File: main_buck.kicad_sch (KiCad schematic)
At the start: 13 parts, among them Q1 IRFB7730PBF, Q2 IRFB7730PBF, U1 IR2109, U2 LM317_TO-220

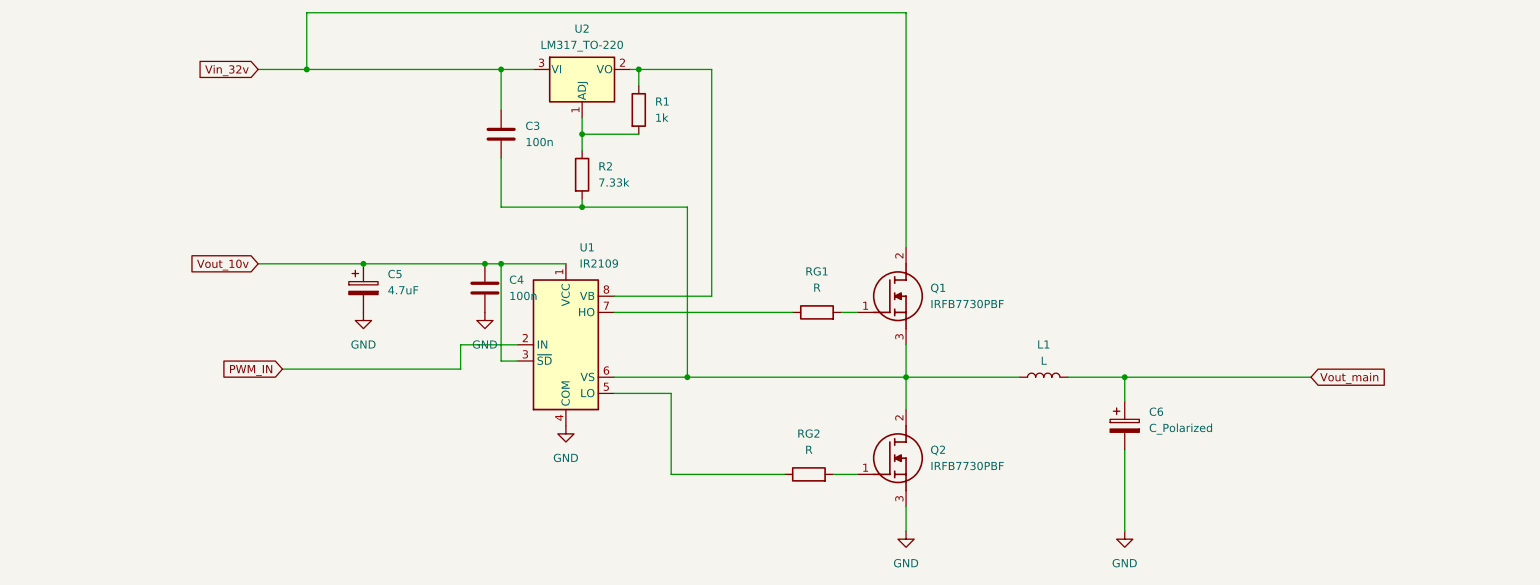
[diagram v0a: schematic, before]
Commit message: zmiana sekcji zasilania digital oraz drivera
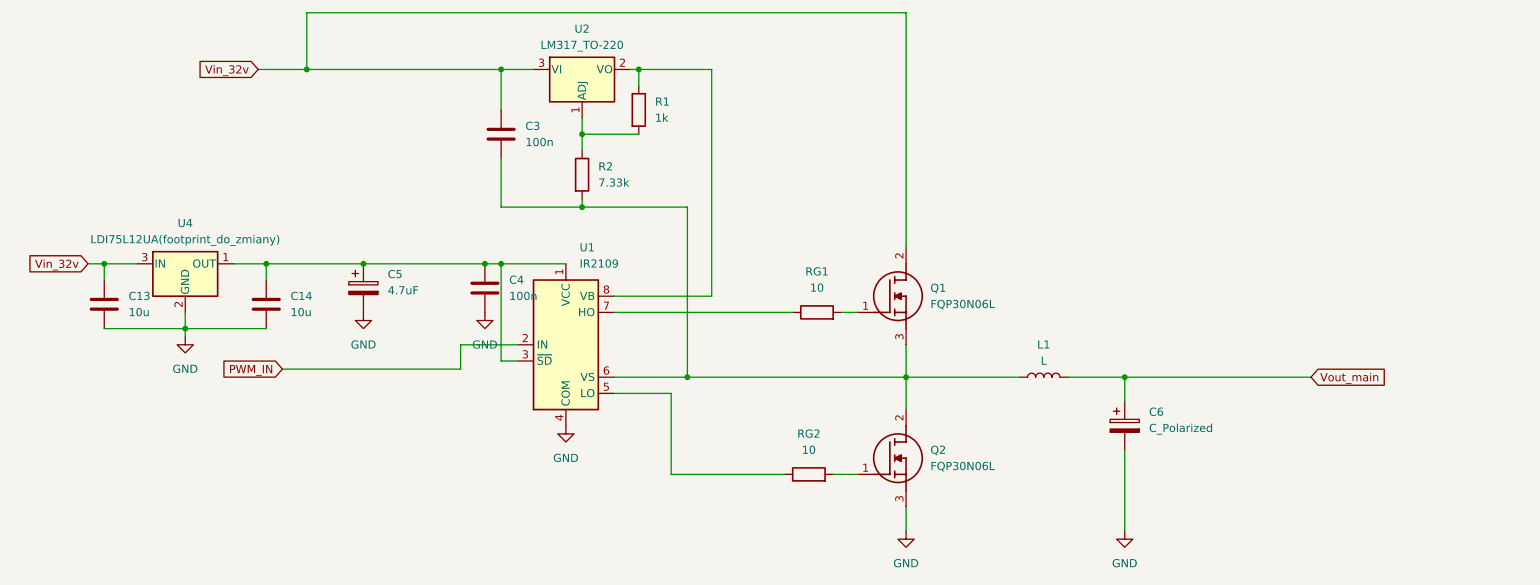
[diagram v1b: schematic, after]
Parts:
- added C13, C14: 10u, symbol Device:C
- added U4: LDI75L12UA(footprint_do_zmiany), Package_TO_SOT_SMD:SOT-89-3, symbol Regulator_Linear:L78L12_SOT89
- Q1, Q2: value IRFB7730PBF -> FQP30N06L
- RG1, RG2: value R -> 10
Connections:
- net GND: now also C13.2, C14.2, U4.2 (GND)
- net Vin_32v: now also C13.1, U4.3 (IN)
- net Vout_10v: no longer names the net of C4.1, C5.1, U1.1 (VCC), U1.3 (~{SD})
- net Vout_10v: now also C14.1, U4.1 (OUT)

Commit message: aktualizacja wartości cewki i kondensatora w przetwornicy głównej
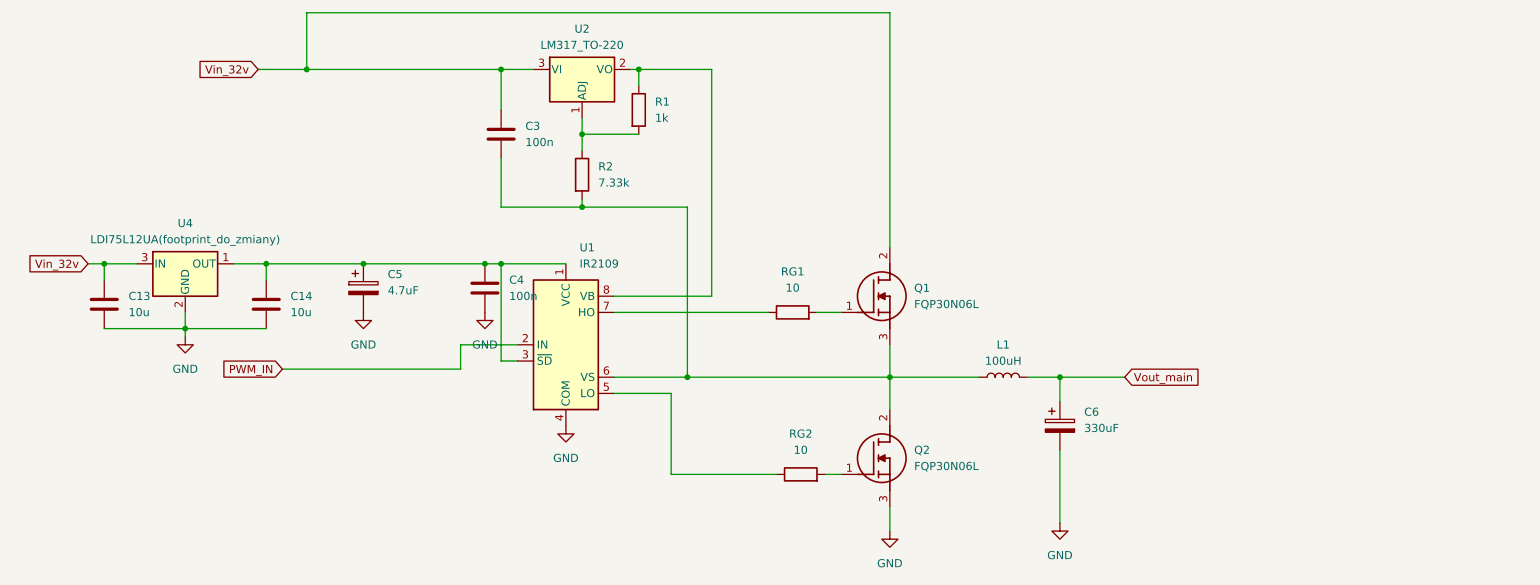
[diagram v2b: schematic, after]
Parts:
- C6: value C_Polarized -> 330uF
- L1: value L -> 100uH
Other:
- moved on the sheet: C6, L1, Q1, Q2, RG1, RG2

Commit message: dodanie testpointów, diody tvs, rezystora pomiarowego
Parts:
- added D3, D4: SMAJ12A, Diode_SMD:D_SMA, symbol Diode:SMAJ12A
- added R_i_mesure: 0.1, symbol Device:R
- added TP_przed_cewka, TP_za_cewka, Vout_main_+, Vout_main_-: Conn_01x01_Pin, symbol Connector:Conn_01x01_Pin
- added fuze_out: Fuse, symbol Device:Fuse
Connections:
- net GND: now also D3.2 (A2), R_i_mesure.1
- net Vout_main: now also fuze_out.2; no longer C6.1, L1.2
- net at C3.2, L1.1, Q1.3 (S)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: now also D4.2 (A2), TP_przed_cewka.1 (Pin_1)
- net at R1.1, U1.8 (VB), U2.2 (VO): now also D4.1 (A1)
- net at C14.1, C4.1, C5.1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: now also D3.1 (A1)
- new net OUT_GND_i_mesure: R_i_mesure.2, Vout_main_-.1 (Pin_1)
- new net Vinm: C6.1, L1.2, TP_za_cewka.1 (Pin_1), Vout_main_+.1 (Pin_1), fuze_out.1

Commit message: dodanie footprintów do main buck (jeszcze driver i razystor bramek) poprawiony pinout LDI75L12UA, dodane footprinty do digital power
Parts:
- removed U2: LM317_TO-220, Package_TO_SOT_THT:TO-220-3_Vertical, symbol Regulator_Linear:LM317_TO-220
- removed U4: LDI75L12UA(footprint_do_zmiany), Package_TO_SOT_SMD:SOT-89-3, symbol Regulator_Linear:L78L12_SOT89
- added U4: LM317_TO-263, Package_TO_SOT_SMD:TO-263-2, symbol Regulator_Linear:LM317_TO-263
- added U8: LDI75L12UA, Package_TO_SOT_SMD:SOT-89-3_Handsoldering, symbol Regulator_Linear:L78L12_SOT89
- C13, C14, C3, C4: footprint (none) -> Capacitor_SMD:C_0805_2012Metric_Pad1.18x1.45mm_HandSolder
- C5: footprint (none) -> Capacitor_SMD:CP_Elec_4x5.8
- C6: footprint (none) -> Capacitor_SMD:CP_Elec_18x17.5
- L1: footprint (none) -> Inductor_THT:L_Toroid_Vertical_L41.9mm_W19.1mm_P15.80mm_Vishay_TJ7
- Q1, Q2: footprint TO254P483X1016X1994-3P -> Package_TO_SOT_THT:TO-220-3_Vertical
- R1, R2: footprint (none) -> Resistor_SMD:R_0805_2012Metric_Pad1.20x1.40mm_HandSolder
- R_i_mesure: footprint (none) -> Resistor_SMD:R_2512_6332Metric_Pad1.40x3.35mm_HandSolder
- TP_przed_cewka, TP_za_cewka: footprint (none) -> Connector_PinHeader_2.54mm:PinHeader_1x01_P2.54mm_Vertical
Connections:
- net GND: now also U8.1 (GND)
- net Vin_32v: now also U4.3 (VI), U8.2 (IN)
- net at D4.1 (A1), R1.1, U1.8 (VB): now also U4.2 (VO)
- net at R1.2, R2.1: now also U4.1 (ADJ)
- net at C14.1, C4.1, C5.1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: now also U8.3 (OUT)

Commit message: Dodanie brakującego połączenia do przycisków enkoderów
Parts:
- renumbered R_i_mesure to R_i_mesure1, TP_przed_cewka to TP_przed_cewka1, TP_za_cewka to TP_za_cewka1, Vout_main_+ to Vout_main_+1, Vout_main_- to Vout_main_-1, fuze_out to fuze_out1
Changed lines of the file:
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@@
 		(dnp no)
 		(fields_autoplaced yes)
-		(property "Reference" "#PWR?"
+		(property "Reference" "#PWR029"
 			(at 80.01 80.01 0)
 			(hide yes)
@@
 			(project "zasilacz_projekt_kompetencyjny"
 				(path "/e9ad3936-200e-4b7c-85fb-533ca6ea54fd/26dc2768-c620-4b2b-8cbb-3a4c93fe0399"
-					(reference "#PWR?")
+					(reference "#PWR029")
 					(unit 1)
 				)
@@
 		(dnp no)
 		(fields_autoplaced yes)
-		(property "Reference" "#PWR?"
+		(property "Reference" "#PWR031"
 			(at 189.23 113.03 0)
 			(hide yes)
@@
 			(project "zasilacz_projekt_kompetencyjny"
 				(path "/e9ad3936-200e-4b7c-85fb-533ca6ea54fd/26dc2768-c620-4b2b-8cbb-3a4c93fe0399"
-					(reference "#PWR?")
+					(reference "#PWR031")
 					(unit 1)
 				)
@@
 		(dnp no)
 		(fields_autoplaced yes)
-		(property "Reference" "#PWR?"
+		(property "Reference" "#PWR030"
 			(at 99.06 80.01 0)
 			(hide yes)
@@
 			(project "zasilacz_projekt_kompetencyjny"
 				(path "/e9ad3936-200e-4b7c-85fb-533ca6ea54fd/26dc2768-c620-4b2b-8cbb-3a4c93fe0399"
-					(reference "#PWR?")
+					(reference "#PWR030")
 					(unit 1)
 				)
@@
 		(dnp no)
 		(fields_autoplaced yes)
-		(property "Reference" "TP_za_cewka"
+		(property "Reference" "TP_za_cewka1"
 			(at 187.96 76.8349 90)
 			(show_name no)
@@
 			(project "zasilacz_projekt_kompetencyjny"
 				(path "/e9ad3936-200e-4b7c-85fb-533ca6ea54fd/26dc2768-c620-4b2b-8cbb-3a4c93fe0399"
-					(reference "TP_za_cewka")
+					(reference "TP_za_cewka1")
 					(unit 1)
 				)
@@
 		(dnp no)
 		(fields_autoplaced yes)
-		(property "Reference" "R_i_mesure"
+		(property "Reference" "R_i_mesure1"
 			(at 214.63 100.33 90)
 			(show_name no)
@@
 			(project "zasilacz_projekt_kompetencyjny"
 				(path "/e9ad3936-200e-4b7c-85fb-533ca6ea54fd/26dc2768-c620-4b2b-8cbb-3a4c93fe0399"
-					(reference "R_i_mesure")
+					(reference "R_i_mesure1")
 					(unit 1)
 				)
@@
 		(dnp no)
 		(fields_autoplaced yes)
-		(property "Reference" "fuze_out"
+		(property "Reference" "fuze_out1"
 			(at 237.49 77.47 90)
 			(show_name no)
@@
 			(project "zasilacz_projekt_kompetencyjny"
 				(path "/e9ad3936-200e-4b7c-85fb-533ca6ea54fd/26dc2768-c620-4b2b-8cbb-3a4c93fe0399"
-					(reference "fuze_out")
+					(reference "fuze_out1")
 					(unit 1)
 				)
@@
 		(dnp no)
 		(fields_autoplaced yes)
-		(property "Reference" "Vout_main_-"
+		(property "Reference" "Vout_main_-1"
 			(at 233.68 109.8549 90)
 			(show_name no)
@@
 			(project "zasilacz_projekt_kompetencyjny"
 				(path "/e9ad3936-200e-4b7c-85fb-533ca6ea54fd/26dc2768-c620-4b2b-8cbb-3a4c93fe0399"
-					(reference "Vout_main_-")
+					(reference "Vout_main_-1")
 					(unit 1)
 				)
@@
 		(dnp no)
 		(fields_autoplaced yes)
-		(property "Reference" "TP_przed_cewka"
+		(property "Reference" "TP_przed_cewka1"
 			(at 168.91 76.8349 90)
 			(show_name no)
@@
 			(project "zasilacz_projekt_kompetencyjny"
 				(path "/e9ad3936-200e-4b7c-85fb-533ca6ea54fd/26dc2768-c620-4b2b-8cbb-3a4c93fe0399"
-					(reference "TP_przed_cewka")
+					(reference "TP_przed_cewka1")
 					(unit 1)
 				)
@@
 		(dnp no)
 		(fields_autoplaced yes)
-		(property "Reference" "Vout_main_+"
+		(property "Reference" "Vout_main_+1"
 			(at 218.44 75.5649 90)
 			(show_name no)
@@
 			(project "zasilacz_projekt_kompetencyjny"
 				(path "/e9ad3936-200e-4b7c-85fb-533ca6ea54fd/26dc2768-c620-4b2b-8cbb-3a4c93fe0399"
-					(reference "Vout_main_+")
-					(unit 1)
-				)
+					(reference "Vout_main_+1")
+					(unit 1)
+				)

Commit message: Przydzielenie brakujących footprintów dla części cyfrowej oprócz enkoderów
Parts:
- RG1, RG2: footprint (none) -> Resistor_SMD:R_0805_2012Metric_Pad1.20x1.40mm_HandSolder
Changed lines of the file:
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@@
 			)
 		)
-		(property "Footprint" ""
+		(property "Footprint" "Resistor_SMD:R_0805_2012Metric_Pad1.20x1.40mm_HandSolder"
 			(at 148.59 100.838 90)
 			(hide yes)
@@
 			)
 		)
-		(property "Footprint" ""
+		(property "Footprint" "Resistor_SMD:R_0805_2012Metric_Pad1.20x1.40mm_HandSolder"
 			(at 147.32 75.438 90)
 			(hide yes)

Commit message: walidacja schematu, dodanie footprintu do drivera, ERC
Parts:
- U1: footprint (none) -> IR2109:SOIC127P600X175-8N
- Vout_main_+1, Vout_main_-1: footprint (none) -> Connector_Wire:SolderWire-1.5sqmm_1x01_D1.7mm_OD3mm
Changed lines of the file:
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@@
 	)
 	(junction
+		(at 111.76 93.98)
+		(diameter 0)
+		(color 0 0 0 0)
+	)
+	(junction
 		(at 130.81 83.82)
 		(diameter 0)
@@
 	(wire
 		(pts
+			(xy 111.76 96.52) (xy 111.76 93.98)
+		)
+		(stroke
+			(width 0)
+			(type default)
+		)
+	)
+	(wire
+		(pts
 			(xy 114.3 43.18) (xy 114.3 45.72)
 		)
@@
 	(wire
 		(pts
+			(xy 111.76 93.98) (xy 111.76 91.44)
+		)
+		(stroke
+			(width 0)
+			(type default)
+		)
+	)
+	(wire
+		(pts
 			(xy 39.37 76.2) (xy 52.07 76.2)
 		)
@@
 	)
 	(symbol
+		(lib_id "power:PWR_FLAG")
+		(at 111.76 93.98 270)
+		(unit 1)
+		(body_style 1)
+		(exclude_from_sim no)
+		(in_bom yes)
+		(on_board yes)
+		(in_pos_files yes)
+		(dnp no)
+		(fields_autoplaced yes)
+		(property "Reference" "#FLG05"
+			(at 113.665 93.98 0)
+			(hide yes)
+			(show_name no)
+			(do_not_autoplace no)
+			(effects
+				(font
+					(size 1.27 1.27)
+				)
+			)
+		)
+		(property "Value" "PWR_FLAG"
+			(at 115.57 93.9799 90)
+			(show_name no)
+			(do_not_autoplace no)
+			(effects
+				(font
+					(size 1.27 1.27)
+				)
+				(justify left)
+			)
+		)
+		(property "Footprint" ""
+			(at 111.76 93.98 0)
+			(hide yes)
+			(show_name no)
+			(do_not_autoplace no)
+			(effects
+				(font
+					(size 1.27 1.27)
+				)
+			)
+		)
+		(property "Datasheet" ""
+			(at 111.76 93.98 0)
+			(hide yes)
+			(show_name no)
+			(do_not_autoplace no)
+			(effects
+				(font
+					(size 1.27 1.27)
+				)
+			)
+		)
+		(property "Description" "Special symbol for telling ERC where power comes from"
+			(at 111.76 93.98 0)
+			(hide yes)
+			(show_name no)
+			(do_not_autoplace no)
+			(effects
+				(font
+					(size 1.27 1.27)
+				)
+			)
+		)
+		(pin "1"
+		)
+		(instances
+			(project "zasilacz_projekt_kompetencyjny"
+				(path "/e9ad3936-200e-4b7c-85fb-533ca6ea54fd/26dc2768-c620-4b2b-8cbb-3a4c93fe0399"
+					(reference "#FLG05")
+					(unit 1)
+				)
+			)
+		)
+	)
+	(symbol
 		(lib_id "Device:C")
 		(at 99.06 69.85 0)
@@
 	(symbol
 		(lib_id "power:GND")
-		(at 111.76 91.44 0)
+		(at 111.76 96.52 0)
 		(unit 1)
 		(body_style 1)
@@
 		(fields_autoplaced yes)
 		(property "Reference" "#PWR01"
-			(at 111.76 97.79 0)
+			(at 111.76 102.87 0)
 			(hide yes)
 			(show_name no)
@@
 		)
 		(property "Value" "GND"
-			(at 111.76 96.52 0)
+			(at 111.76 101.6 0)
 			(show_name no)
 			(do_not_autoplace no)
@@
 		)
 		(property "Footprint" ""
-			(at 111.76 91.44 0)
+			(at 111.76 96.52 0)
 			(hide yes)
 			(show_name no)
@@
 		)
 		(property "Datasheet" ""
-			(at 111.76 91.44 0)
+			(at 111.76 96.52 0)
 			(hide yes)
 			(show_name no)
@@
 		)
 		(property "Description" "Power symbol creates a global label with name \"GND\" , ground"
-			(at 111.76 91.44 0)
+			(at 111.76 96.52 0)
 			(hide yes)
 			(show_name no)
@@
 			)
 		)
-		(property "Footprint" ""
+		(property "Footprint" "Connector_Wire:SolderWire-1.5sqmm_1x01_D1.7mm_OD3mm"
 			(at 232.41 111.76 0)
 			(hide yes)
@@
 			)
 		)
-		(property "Footprint" ""
+		(property "Footprint" "IR2109:SOIC127P600X175-8N"
 			(at 111.76 78.74 0)
 			(hide yes)
@@
 			)
 		)
-		(property "Footprint" ""
+		(property "Footprint" "Connector_Wire:SolderWire-1.5sqmm_1x01_D1.7mm_OD3mm"
 			(at 217.17 76.2 0)
 			(hide yes)
